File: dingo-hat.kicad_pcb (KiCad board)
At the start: 2 copper layers, 65 x 56 mm, 87 parts, among them J1 LiPo-Power, J10 PJ-038BH, J11 Bypass-Power, J12 Chassis-Out, J13 i2c_display, J14 NEOPIXEL, J15 MPU-9250, J2 Raspberry_Pi_2_3, J201 Bootstrap, J24 3mm_Mount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

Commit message: Changing barrel jack to be 2.1ID, 5.5OD. Needs double check to close issue (28).
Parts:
- removed C201: 100nF, Capacitor_SMD:C_0603_1608Metric_Pad1.05x0.95mm_HandSolder
- removed C203: 1uF, Capacitor_SMD:C_0603_1608Metric_Pad1.05x0.95mm_HandSolder
- removed J201: Bootstrap, Pin_Headers:Pin_Header_Straight_1x02_Pitch1.27mm
- removed R201: 470, Resistor_SMD:R_0603_1608Metric_Pad1.05x0.95mm_HandSolder
- removed R203: 2k7, Resistor_SMD:R_0603_1608Metric_Pad1.05x0.95mm_HandSolder
- removed U201: AP9211, libs:6-UDFN-Exposed-Pad
- added G3: LCA2020Logo.2, libs:logo.LCA.2020.2, F.Cu at (163.5, 70.3)
- added Q201: BSS84, TO_SOT_Packages_SMD:SOT-23, F.Cu at (183.6, 70.8)
- D2: value 30V -> 30V 1A
- J10: value PJ-038BH -> PJ-038AH; footprint libs:CUI_PJ-038BH -> libs:CUI_PJ-038AH
- R204: value 1k -> 1.5k
- RN1: value 220x4 -> 220_Pack04
- U202: value MCP73213T -> MCP73213T-A6BI_MF
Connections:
- D2 pad 2: /LiBatt- -> GND
- J1 pad 2: /LiBatt- -> GND
- R204 pad 1: Net-(R204-Pad1) -> Net-(Q201-Pad3)
- U202 pad 10: Net-(R204-Pad1) -> Net-(Q201-Pad2)
- U203 pad 8: Net-(U203-Pad8) -> /LiPoBatteryMgmt/BalOUT
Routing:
- net /LiBatt-: track 14.0 -> 0.00 mm
- net GND: track 42.6 -> 56.7 mm
- removed copper zone on F.Cu, net /LiBatt-

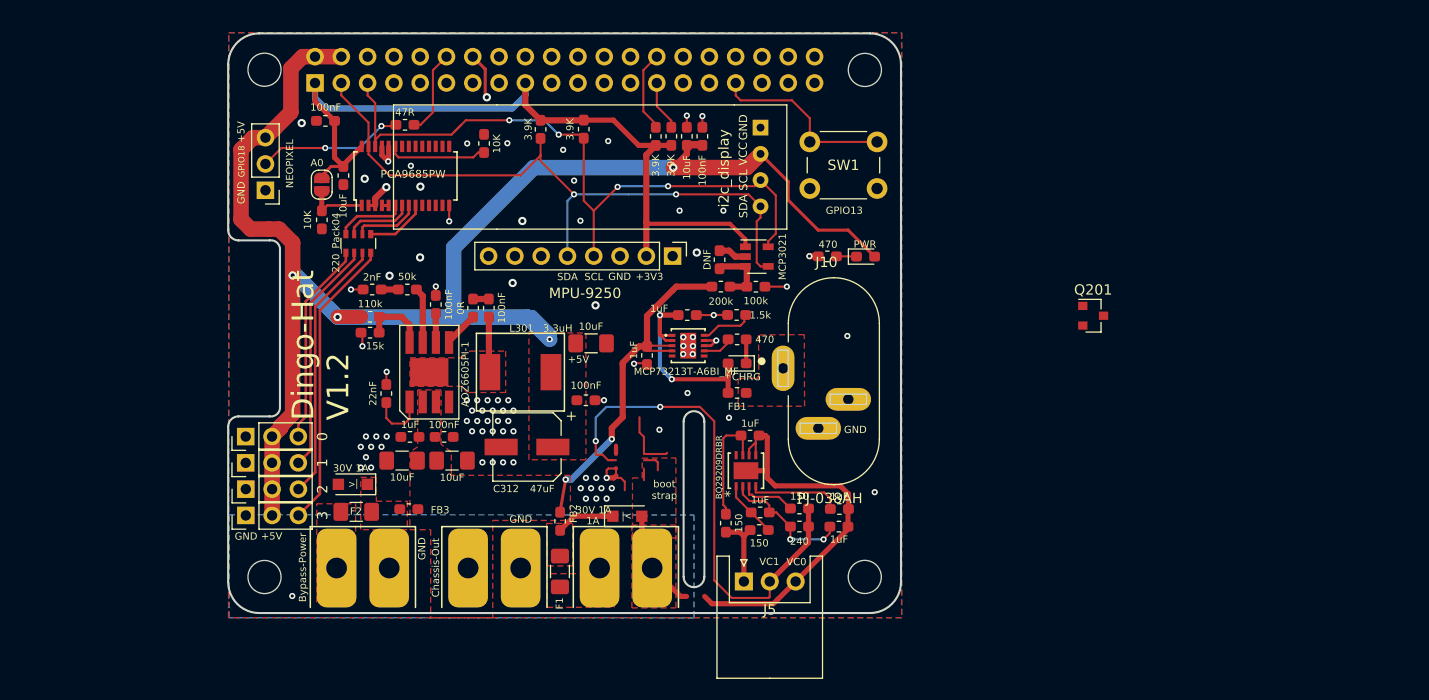
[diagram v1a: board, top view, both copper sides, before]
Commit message: Change mounting holes to M2.5. Closes #29.
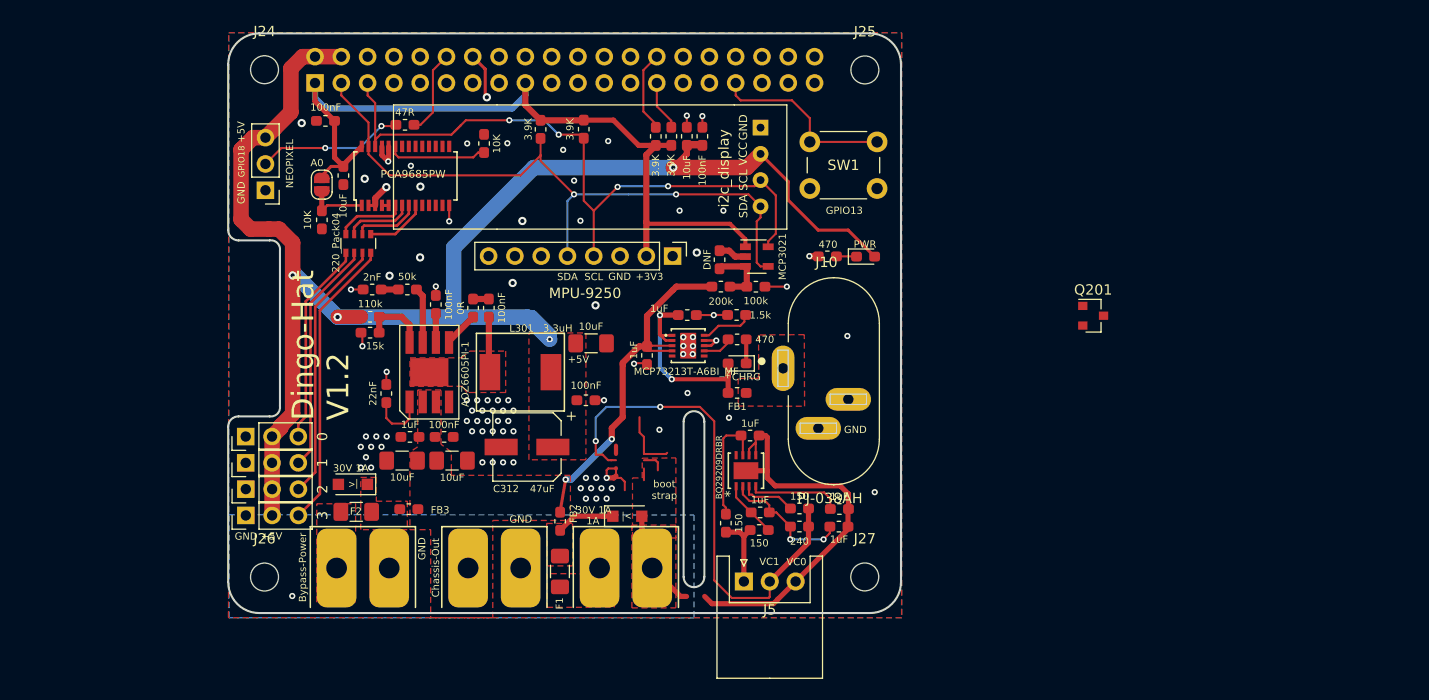
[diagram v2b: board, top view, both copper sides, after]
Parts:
- J24, J25, J26, J27: value 3mm_Mount -> M2.5_Mount; footprint MountingHole:MountingHole_3.2mm_M3 -> Mounting_Holes:MountingHole_2.7mm_M2.5
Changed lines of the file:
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@@
     (uvia_drill 0.1)
   )
+  (module Mounting_Holes:MountingHole_2.7mm_M2.5 (layer F.Cu)
+    (at 161.5 96.01)
+    (descr "Mounting Hole 2.7mm, no annular, M2.5")
+    (tags "mounting hole 2.7mm no annular m2.5")
+    (attr virtual)
+    (fp_text reference J27 (at 0 -3.7) (layer F.SilkS)
+      (effects (font (size 1 1) (thickness 0.15)))
+    )
+    (fp_text value M2.5_Mount (at 0 3.7) (layer F.Fab)
+      (effects (font (size 1 1) (thickness 0.15)))
+    )
+    (fp_text user %R (at 0.3 0) (layer F.Fab)
+      (effects (font (size 1 1) (thickness 0.15)))
+    )
+    (fp_circle (center 0 0) (end 2.7 0) (layer Cmts.User) (width 0.15))
+    (fp_circle (center 0 0) (end 2.95 0) (layer F.CrtYd) (width 0.05))
+    (pad 1 np_thru_hole circle (at 0 0) (size 2.7 2.7) (drill 2.7) (layers *.Cu *.Mask)
+      (net 55 "Net-(J27-Pad1)"))
+  )
+  (module Mounting_Holes:MountingHole_2.7mm_M2.5 (layer F.Cu)
+    (at 103.51 96.02)
+    (descr "Mounting Hole 2.7mm, no annular, M2.5")
+    (tags "mounting hole 2.7mm no annular m2.5")
+    (attr virtual)
+    (fp_text reference J26 (at 0 -3.7) (layer F.SilkS)
+      (effects (font (size 1 1) (thickness 0.15)))
+    )
+    (fp_text value M2.5_Mount (at 0 3.7) (layer F.Fab)
+      (effects (font (size 1 1) (thickness 0.15)))
+    )
+    (fp_text user %R (at 0.3 0) (layer F.Fab)
+      (effects (font (size 1 1) (thickness 0.15)))
+    )
+    (fp_circle (center 0 0) (end 2.7 0) (layer Cmts.User) (width 0.15))
+    (fp_circle (center 0 0) (end 2.95 0) (layer F.CrtYd) (width 0.05))
+    (pad 1 np_thru_hole circle (at 0 0) (size 2.7 2.7) (drill 2.7) (layers *.Cu *.Mask)
+      (net 54 "Net-(J26-Pad1)"))
+  )
+  (module Mounting_Holes:MountingHole_2.7mm_M2.5 (layer F.Cu)
+    (at 161.51 47.03)
+    (descr "Mounting Hole 2.7mm, no annular, M2.5")
+    (tags "mounting hole 2.7mm no annular m2.5")
+    (attr virtual)
+    (fp_text reference J25 (at 0 -3.7) (layer F.SilkS)
+      (effects (font (size 1 1) (thickness 0.15)))
+    )
+    (fp_text value M2.5_Mount (at 0 3.7) (layer F.Fab)
+      (effects (font (size 1 1) (thickness 0.15)))
+    )
+    (fp_text user %R (at 0.3 0) (layer F.Fab)
+      (effects (font (size 1 1) (thickness 0.15)))
+    )
+    (fp_circle (center 0 0) (end 2.7 0) (layer Cmts.User) (width 0.15))
+    (fp_circle (center 0 0) (end 2.95 0) (layer F.CrtYd) (width 0.05))
+    (pad 1 np_thru_hole circle (at 0 0) (size 2.7 2.7) (drill 2.7) (layers *.Cu *.Mask)
+      (net 53 "Net-(J25-Pad1)"))
+  )
+  (module Mounting_Holes:MountingHole_2.7mm_M2.5 (layer F.Cu)
+    (at 103.51 47.01)
+    (descr "Mounting Hole 2.7mm, no annular, M2.5")
+    (tags "mounting hole 2.7mm no annular m2.5")
+    (attr virtual)
+    (fp_text reference J24 (at 0 -3.7) (layer F.SilkS)
+      (effects (font (size 1 1) (thickness 0.15)))
+    )
+    (fp_text value M2.5_Mount (at 0 3.7) (layer F.Fab)
+      (effects (font (size 1 1) (thickness 0.15)))
+    )
+    (fp_text user %R (at 0.3 0) (layer F.Fab)
+      (effects (font (size 1 1) (thickness 0.15)))
+    )
+    (fp_circle (center 0 0) (end 2.7 0) (layer Cmts.User) (width 0.15))
+    (fp_circle (center 0 0) (end 2.95 0) (layer F.CrtYd) (width 0.05))
+    (pad 1 np_thru_hole circle (at 0 0) (size 2.7 2.7) (drill 2.7) (layers *.Cu *.Mask)
+      (net 52 "Net-(J24-Pad1)"))
+  )
   (module TO_SOT_Packages_SMD:SOT-23 (layer F.Cu)
     (at 183.565001 70.775001)
@@
     )
   )
-  (module MountingHole:MountingHole_3.2mm_M3 (layer F.Cu)
-    (at 161.51 47.03)
-    (descr "Mounting Hole 3.2mm, no annular, M3")
-    (tags "mounting hole 3.2mm no annular m3")
-    (attr virtual)
-    (fp_text reference J25 (at 0 -4.2) (layer F.SilkS) hide
-      (effects (font (size 1 1) (thickness 0.15)))
-    )
-    (fp_text value 3mm_Mount (at 0 4.2) (layer F.Fab) hide
-      (effects (font (size 1 1) (thickness 0.15)))
-    )
-    (fp_text user %R (at 0.3 0) (layer F.Fab)
-      (effects (font (size 1 1) (thickness 0.15)))
-    )
-    (fp_circle (center 0 0) (end 3.2 0) (layer Cmts.User) (width 0.15))
-    (fp_circle (center 0 0) (end 3.45 0) (layer F.CrtYd) (width 0.05))
-    (pad 1 np_thru_hole circle (at 0 0) (size 3.2 3.2) (drill 3.2) (layers *.Cu *.Mask)
-      (net 53 "Net-(J25-Pad1)"))
-  )
   (module libs:SolderWirePad_2x_5.08mm_14-18AWG-2mmDrill (layer F.Cu)
     (at 138.42 95.15)
@@
     )
   )
-  (module MountingHole:MountingHole_3.2mm_M3 (layer F.Cu)
-    (at 103.51 47.01)
-    (descr "Mounting Hole 3.2mm, no annular, M3")
-    (tags "mounting hole 3.2mm no annular m3")
-    (attr virtual)
-    (fp_text reference J24 (at 0 -4.2) (layer F.SilkS) hide
-      (effects (font (size 1 1) (thickness 0.15)))
-    )
-    (fp_text value 3mm_Mount (at 0 4.2) (layer F.Fab) hide
-      (effects (font (size 1 1) (thickness 0.15)))
-    )
-    (fp_circle (center 0 0) (end 3.45 0) (layer F.CrtYd) (width 0.05))
-    (fp_circle (center 0 0) (end 3.2 0) (layer Cmts.User) (width 0.15))
-    (fp_text user %R (at 0.3 0) (layer F.Fab)
-      (effects (font (size 1 1) (thickness 0.15)))
-    )
-    (pad 1 np_thru_hole circle (at 0 0) (size 3.2 3.2) (drill 3.2) (layers *.Cu *.Mask)
-      (net 52 "Net-(J24-Pad1)"))
-  )
-  (module MountingHole:MountingHole_3.2mm_M3 (layer F.Cu)
-    (at 103.51 96.02)
-    (descr "Mounting Hole 3.2mm, no annular, M3")
-    (tags "mounting hole 3.2mm no annular m3")
-    (attr virtual)
-    (fp_text reference J26 (at 0 -4.2) (layer F.SilkS) hide
-      (effects (font (size 1 1) (thickness 0.15)))
-    )
-    (fp_text value 3mm_Mount (at 0 4.2) (layer F.Fab) hide
-      (effects (font (size 1 1) (thickness 0.15)))
-    )
-    (fp_circle (center 0 0) (end 3.45 0) (layer F.CrtYd) (width 0.05))
-    (fp_circle (center 0 0) (end 3.2 0) (layer Cmts.User) (width 0.15))
-    (fp_text user %R (at 0.3 0) (layer F.Fab)
-      (effects (font (size 1 1) (thickness 0.15)))
-    )
-    (pad 1 np_thru_hole circle (at 0 0) (size 3.2 3.2) (drill 3.2) (layers *.Cu *.Mask)
-      (net 54 "Net-(J26-Pad1)"))
-  )
-  (module MountingHole:MountingHole_3.2mm_M3 (layer F.Cu)
-    (at 161.5 96.01)
-    (descr "Mounting Hole 3.2mm, no annular, M3")
-    (tags "mounting hole 3.2mm no annular m3")
-    (attr virtual)
-    (fp_text reference J27 (at 0 -4.2) (layer F.SilkS) hide
-      (effects (font (size 1 1) (thickness 0.15)))
-    )
-    (fp_text value 3mm_Mount (at 0 4.2) (layer F.Fab) hide
-      (effects (font (size 1 1) (thickness 0.15)))
-    )
-    (fp_text user %R (at 0.3 0) (layer F.Fab)
-      (effects (font (size 1 1) (thickness 0.15)))
-    )
-    (fp_circle (center 0 0) (end 3.2 0) (layer Cmts.User) (width 0.15))
-    (fp_circle (center 0 0) (end 3.45 0) (layer F.CrtYd) (width 0.05))
-    (pad 1 np_thru_hole circle (at 0 0) (size 3.2 3.2) (drill 3.2) (layers *.Cu *.Mask)
-      (net 55 "Net-(J27-Pad1)"))
-  )
   (module Connector_PinHeader_2.54mm:PinHeader_1x08_P2.54mm_Vertical (layer F.Cu)

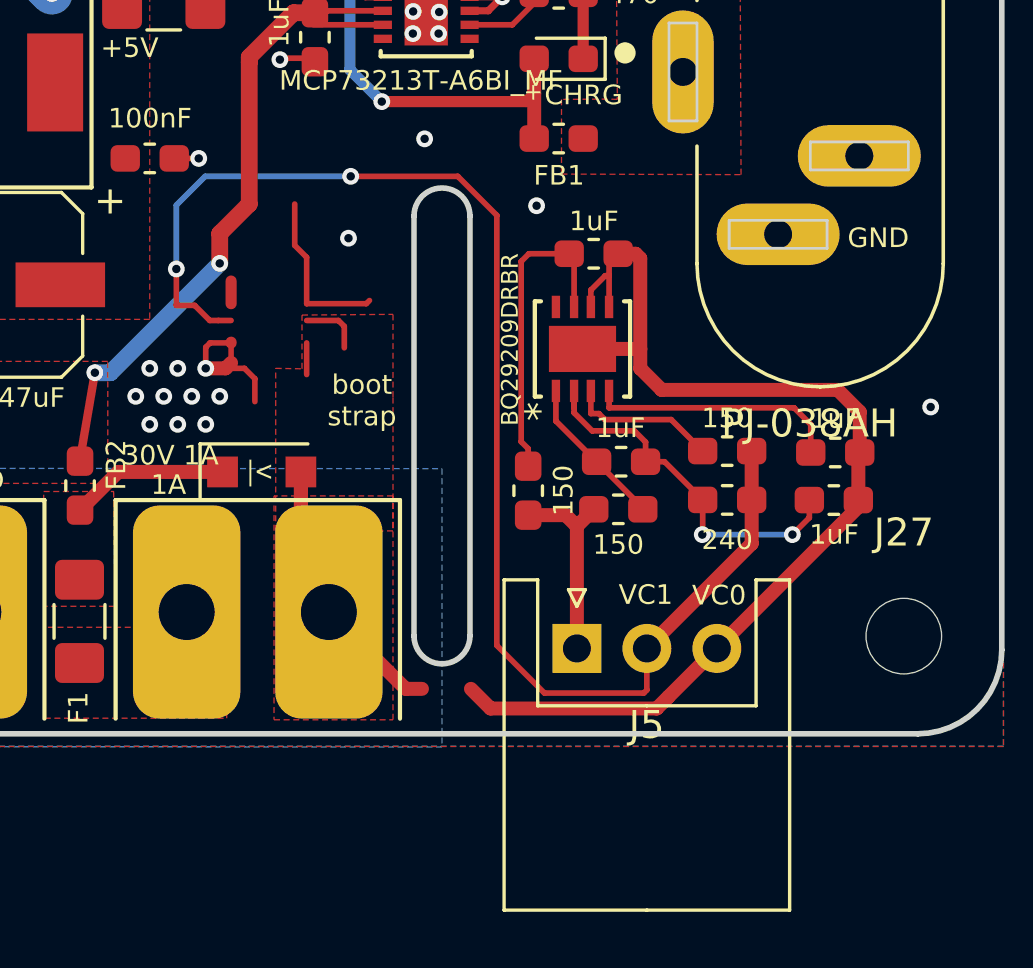
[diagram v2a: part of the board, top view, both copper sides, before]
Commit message: Cleaning up, flipped JST balance. Closes #21.
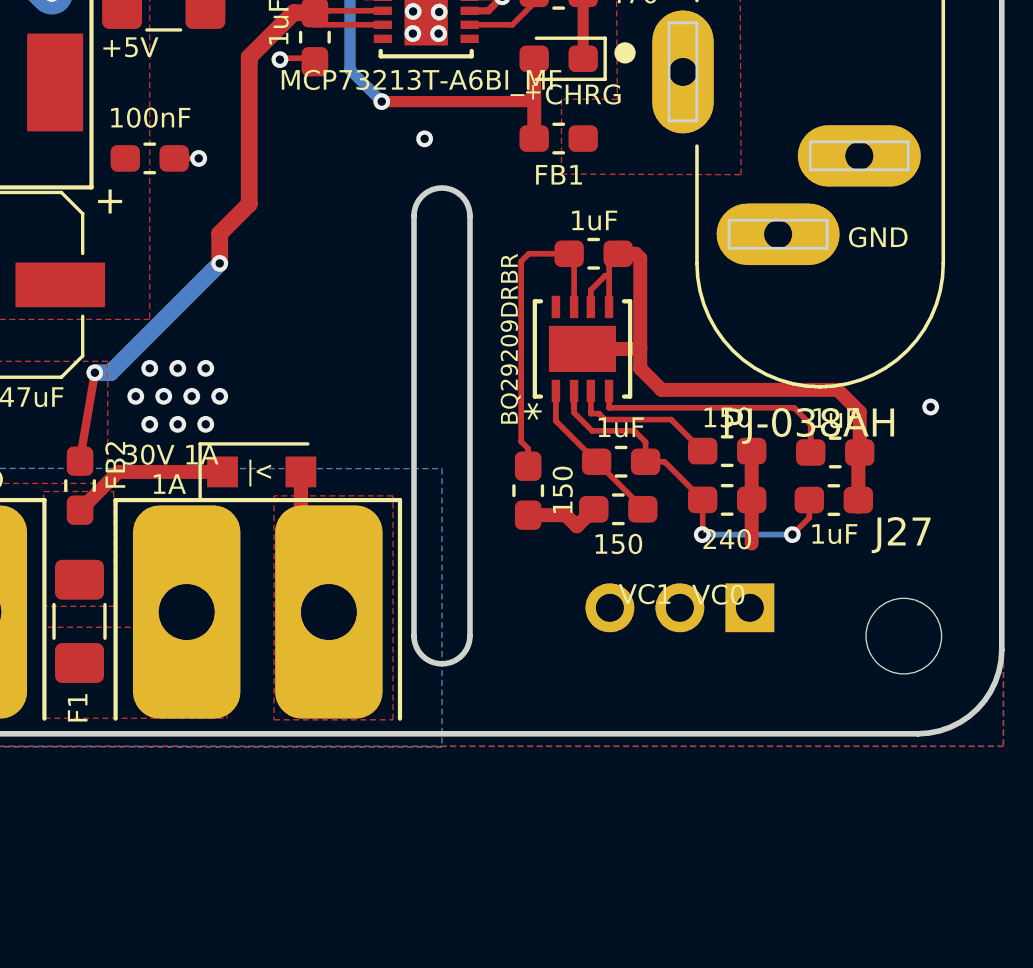
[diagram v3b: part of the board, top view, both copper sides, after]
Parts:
- J5: moved to B.Cu
- moved J5 6.35 mm to (156.0, 95.0), turned to 180 degrees
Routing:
- net /VC1: track 49.8 -> 3.30 mm, vias 2 -> 0
- net /VC0: track 44.0 -> 26.9 mm
- net GND: track 56.7 -> 42.7 mm, vias 89 -> 87
- net Net-(C201-Pad1): track 6.03 -> 0.00 mm
- net /VC2: track 7.12 -> 2.76 mm
- net Net-(U201-Pad4): track 0.81 -> 0.00 mm
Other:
- board text removed: "boot strap"

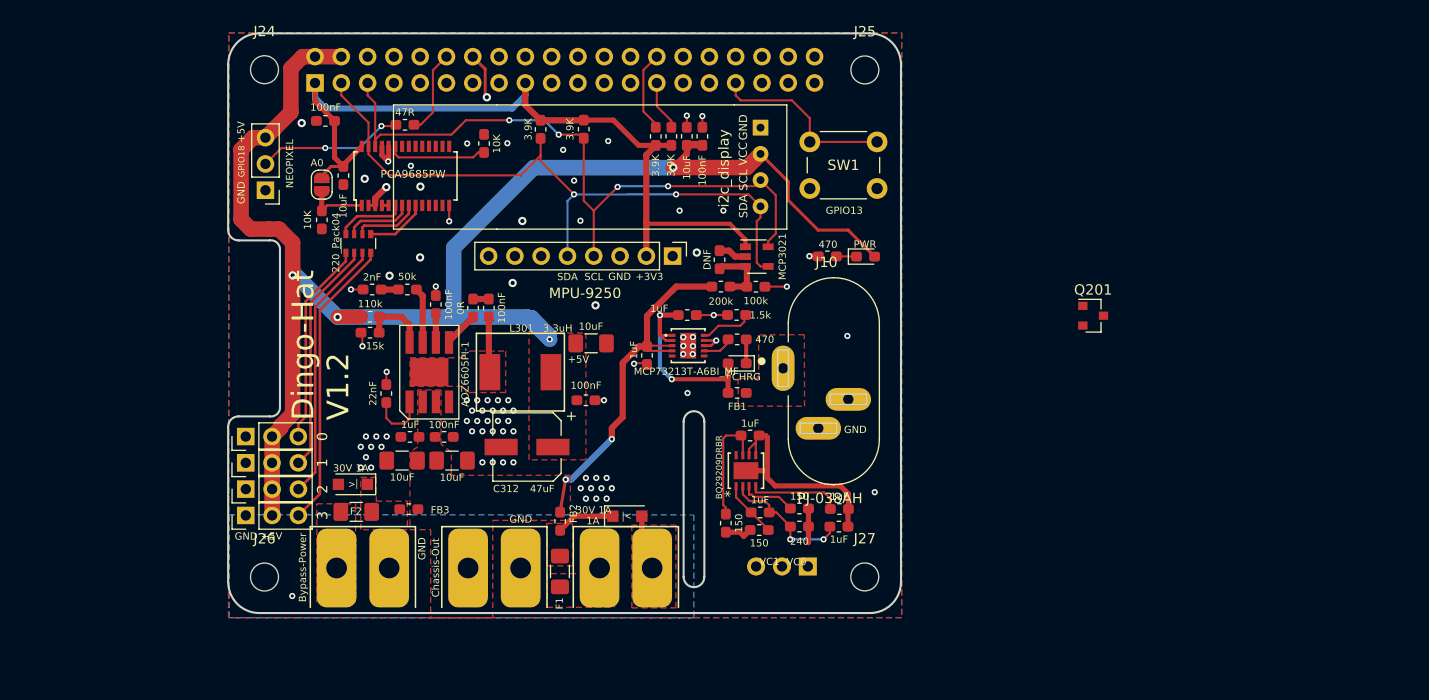
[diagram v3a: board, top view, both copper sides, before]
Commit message: Added second header for OLED referenced in #25, need to place. Added model for barrel jack - may not be perfectly aligned.
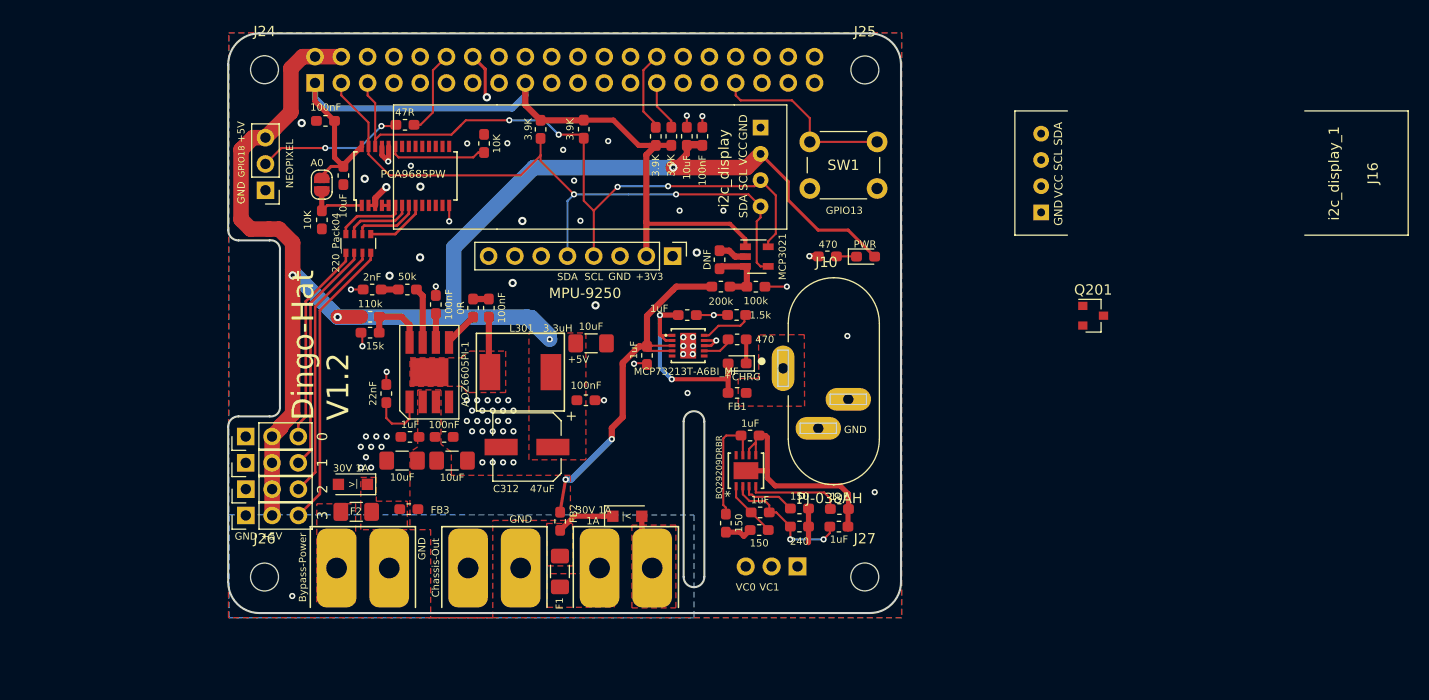
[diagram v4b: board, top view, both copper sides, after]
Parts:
- added J16: i2c_display_1, libs:0.91 OLED, F.Cu at (195.0, 57.0)
- moved J5 1.00 mm to (155.0, 95.0)
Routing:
- net GND: vias 87 -> 77
